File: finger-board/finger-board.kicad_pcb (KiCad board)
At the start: 2 copper layers, 15 x 84 mm, 9 parts, among them IC1 TMAG5253BA1IQDMRR, IC2 TMAG5253BA1IQDMRR, IC3 TMAG5253BA1IQDMRR, IC4 TMAG5253BA1IQDMRR, J1 Conn_01x10_MountingPin, U1 SK6812MINI-E, U2 SK6812MINI-E, U3 SK6812MINI-E, U4 SK6812MINI-E

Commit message: Trace finger-board
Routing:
- net +3.3V: track 7.65 -> 159.4 mm, vias 0 -> 9
- net /CMN: track 5.15 -> 115.3 mm, vias 0 -> 8
- net /DOUT: track 0.00 -> 108.3 mm, vias 0 -> 3
- net +5V: track 6.42 -> 113.8 mm, vias 0 -> 1
- net /EN_4: track 0.00 -> 102.3 mm, vias 0 -> 2
- net GND: track 8.65 -> 85.3 mm, vias 0 -> 15
- net /EN_3: track 0.00 -> 74.9 mm, vias 0 -> 4
- net /EN_2: track 0.00 -> 44.6 mm
- net /D_1: track 0.00 -> 37.1 mm, vias 0 -> 2
- net /D_2: track 0.00 -> 36.1 mm, vias 0 -> 2
- net /D_0: track 4.47 -> 36.1 mm, vias 0 -> 2
- net /DIN: track 0.00 -> 10.2 mm, vias 0 -> 1
- net /EN_1: track 0.00 -> 9.53 mm, vias 0 -> 2
- net (no net): vias 8 -> 0
- added copper zone on B.Cu, net GND
- added copper zone on F.Cu, net GND
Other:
- board text removed: "Production"

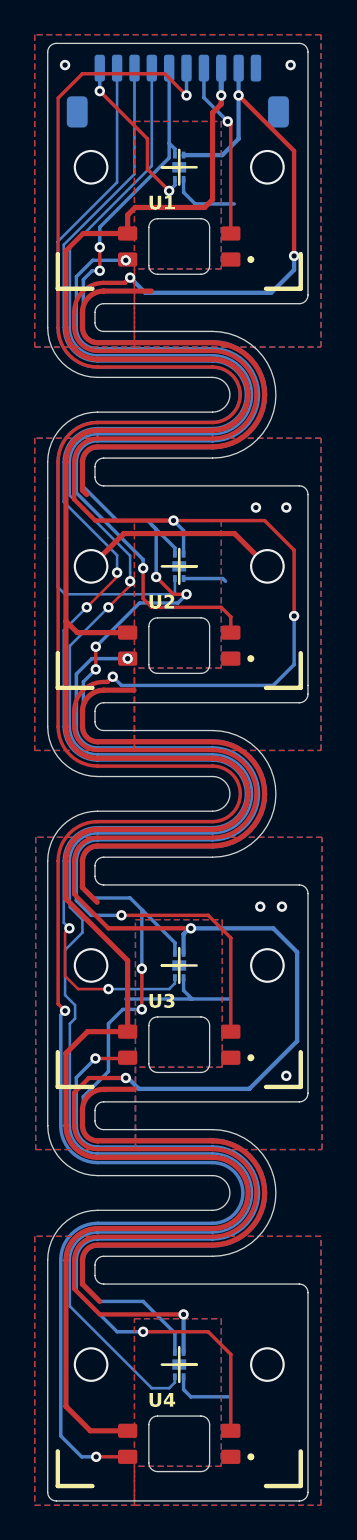
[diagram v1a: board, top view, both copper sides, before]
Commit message: Move SK6812 a bit down on daughter boards
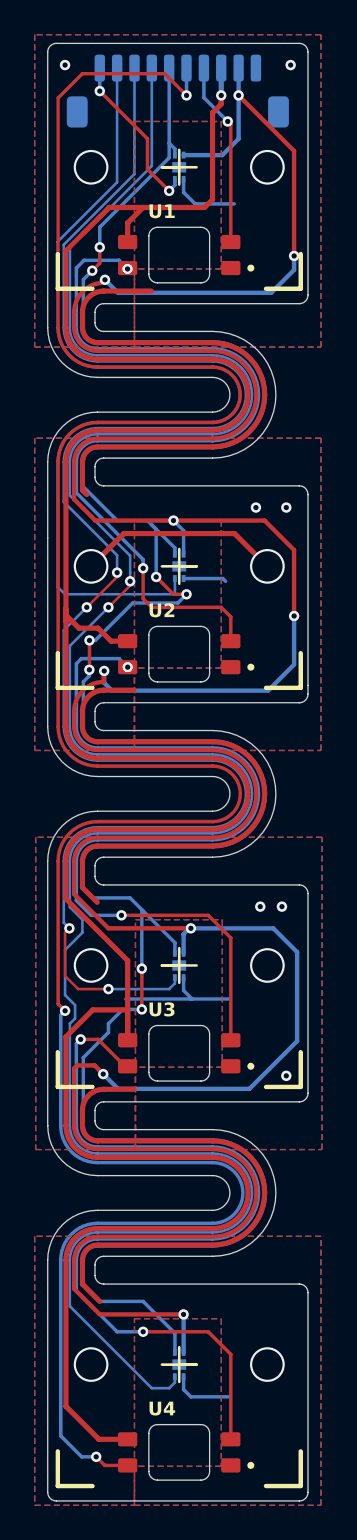
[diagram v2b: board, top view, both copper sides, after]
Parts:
- moved U1 0.49 mm to (143.1, 90.7)
- moved U2 0.49 mm to (143.1, 113.7)
- moved U3 0.49 mm to (143.1, 136.7)
- moved U4 0.49 mm to (143.1, 159.7)
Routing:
- net +5V: track 113.8 -> 120.2 mm
- net /D_2: track 36.1 -> 38.8 mm
- net +3.3V: track 159.4 -> 162.1 mm
- net /D_1: track 37.1 -> 38.1 mm

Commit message: Developer Preview 1
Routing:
- net /CMN: track 115.4 -> 116.3 mm
- net +3.3V: track 162.1 -> 161.4 mm

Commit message: Rename the board to Skadi
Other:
- board text added: "SKADI_FB_REV1.0"
- board text removed: "DV1_FB_REV1.0"
